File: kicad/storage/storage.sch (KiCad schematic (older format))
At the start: 8 parts, among them J1 Conn_02x30_Counter_Clockwise, J6 Conn_01x01, U1 7400, U2 7400, U3 Conn_02x08_Counter_Clockwise

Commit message: Finish storage card
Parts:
- removed J6: Conn_01x01, Connector_PinHeader_2.54mm:PinHeader_1x01_P2.54mm_Vertical, symbol Connector_Generic:Conn_01x01
- added J6: Conn_01x03, Connector_PinHeader_2.54mm:PinHeader_1x03_P2.54mm_Vertical, symbol Connector_Generic:Conn_01x03
- added J7: Conn_01x02, Connector_PinHeader_2.54mm:PinHeader_1x02_P2.54mm_Vertical, symbol Connector_Generic:Conn_01x02
- added R1, R2: R, Resistor_THT:R_Axial_DIN0207_L6.3mm_D2.5mm_P10.16mm_Horizontal, symbol Device:R
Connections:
- net GND: now also J6.1 (Pin_1)
- net WR: now also J1.38 (Pin_38)
- new net: J6.2 (Pin_2), R1.1
- new net: J6.3 (Pin_3), R2.1
- new net: J7.2 (Pin_2), R1.2
- new net: J7.1 (Pin_1), R2.2
- no-connect marks 38 -> 37
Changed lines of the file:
@@
 NoConn ~ 10100 4500
 NoConn ~ 10100 4400
-NoConn ~ 10100 4300
 NoConn ~ 10100 2800
 NoConn ~ 10100 3000
@@
 NoConn ~ 9600 4900
 $Comp
-L Connector_Generic:Conn_01x01 J6
-U 1 1 60BD2C0A
-P 1350 1400
-F 0 "J6" H 1430 1442 50  0000 L CNN
-F 1 "Conn_01x01" H 1430 1351 50  0000 L CNN
-F 2 "Connector_PinHeader_2.54mm:PinHeader_1x01_P2.54mm_Vertical" H 1350 1400 50  0001 C CNN
-F 3 "~" H 1350 1400 50  0001 C CNN
-	1    1350 1400
-	1    0    0    -1
-$EndComp
-Text GLabel 1150 1400 0    50   Input ~ 0
-WR
-$Comp
 L 74xx:7400 U1
 U 2 1 60BD3C08
@@
 Wire Wire Line
 	3150 7300 3450 7300
+Text GLabel 10100 4300 2    50   Input ~ 0
+WR
+$Comp
+L Connector_Generic:Conn_01x03 J6
+U 1 1 60C409E1
+P 2750 1500
+F 0 "J6" H 2830 1542 50  0000 L CNN
+F 1 "Conn_01x03" H 2830 1451 50  0000 L CNN
+F 2 "Connector_PinHeader_2.54mm:PinHeader_1x03_P2.54mm_Vertical" H 2750 1500 50  0001 C CNN
+F 3 "~" H 2750 1500 50  0001 C CNN
+	1    2750 1500
+	1    0    0    -1
+$EndComp
+Text GLabel 2550 1400 0    50   Input ~ 0
+GND
+$Comp
+L Device:R R1
+U 1 1 60C52E56
+P 2400 1500
+F 0 "R1" V 2193 1500 50  0000 C CNN
+F 1 "R" V 2284 1500 50  0000 C CNN
+F 2 "Resistor_THT:R_Axial_DIN0207_L6.3mm_D2.5mm_P10.16mm_Horizontal" V 2330 1500 50  0001 C CNN
+F 3 "~" H 2400 1500 50  0001 C CNN
+	1    2400 1500
+	0    1    1    0
+$EndComp
+$Comp
+L Device:R R2
+U 1 1 60C5383C
+P 2400 1600
+F 0 "R2" V 2193 1600 50  0000 C CNN
+F 1 "R" V 2284 1600 50  0000 C CNN
+F 2 "Resistor_THT:R_Axial_DIN0207_L6.3mm_D2.5mm_P10.16mm_Horizontal" V 2330 1600 50  0001 C CNN
+F 3 "~" H 2400 1600 50  0001 C CNN
+	1    2400 1600
+	0    1    1    0
+$EndComp
+$Comp
+L Connector_Generic:Conn_01x02 J7
+U 1 1 60C55150
+P 2050 1600
+F 0 "J7" H 1968 1275 50  0000 C CNN
+F 1 "Conn_01x02" H 1968 1366 50  0000 C CNN
+F 2 "Connector_PinHeader_2.54mm:PinHeader_1x02_P2.54mm_Vertical" H 2050 1600 50  0001 C CNN
+F 3 "~" H 2050 1600 50  0001 C CNN
+	1    2050 1600
+	-1   0    0    1
+$EndComp
 $EndSCHEMATC

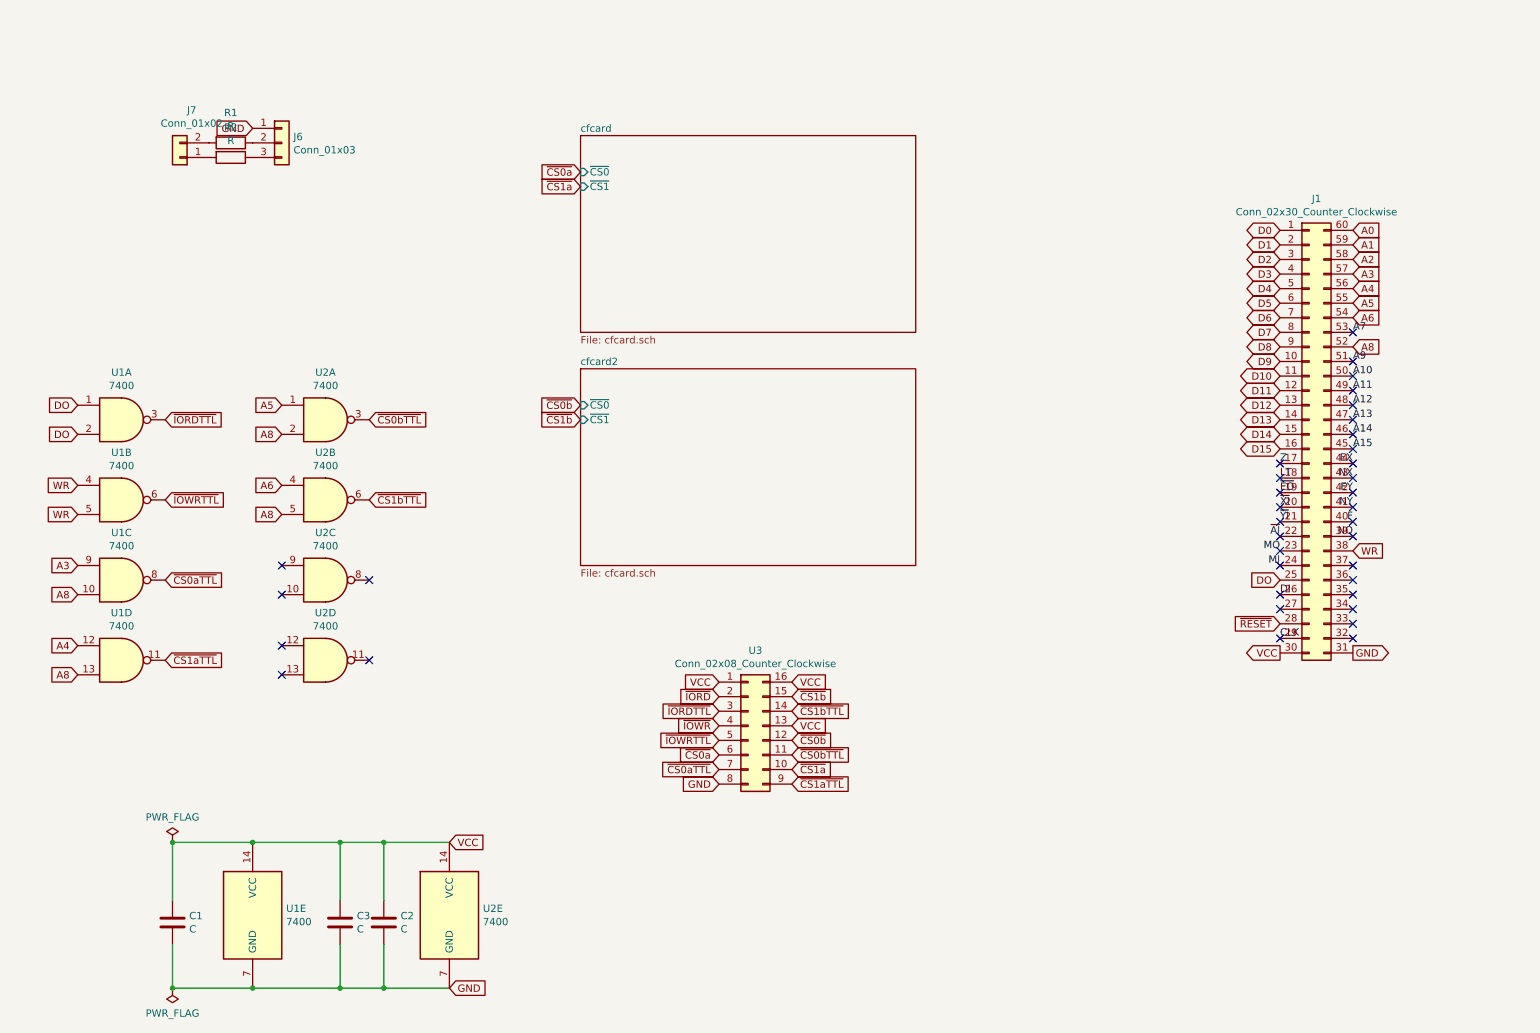
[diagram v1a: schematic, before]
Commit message: Add 74HCT245 bus transceivers to storage card
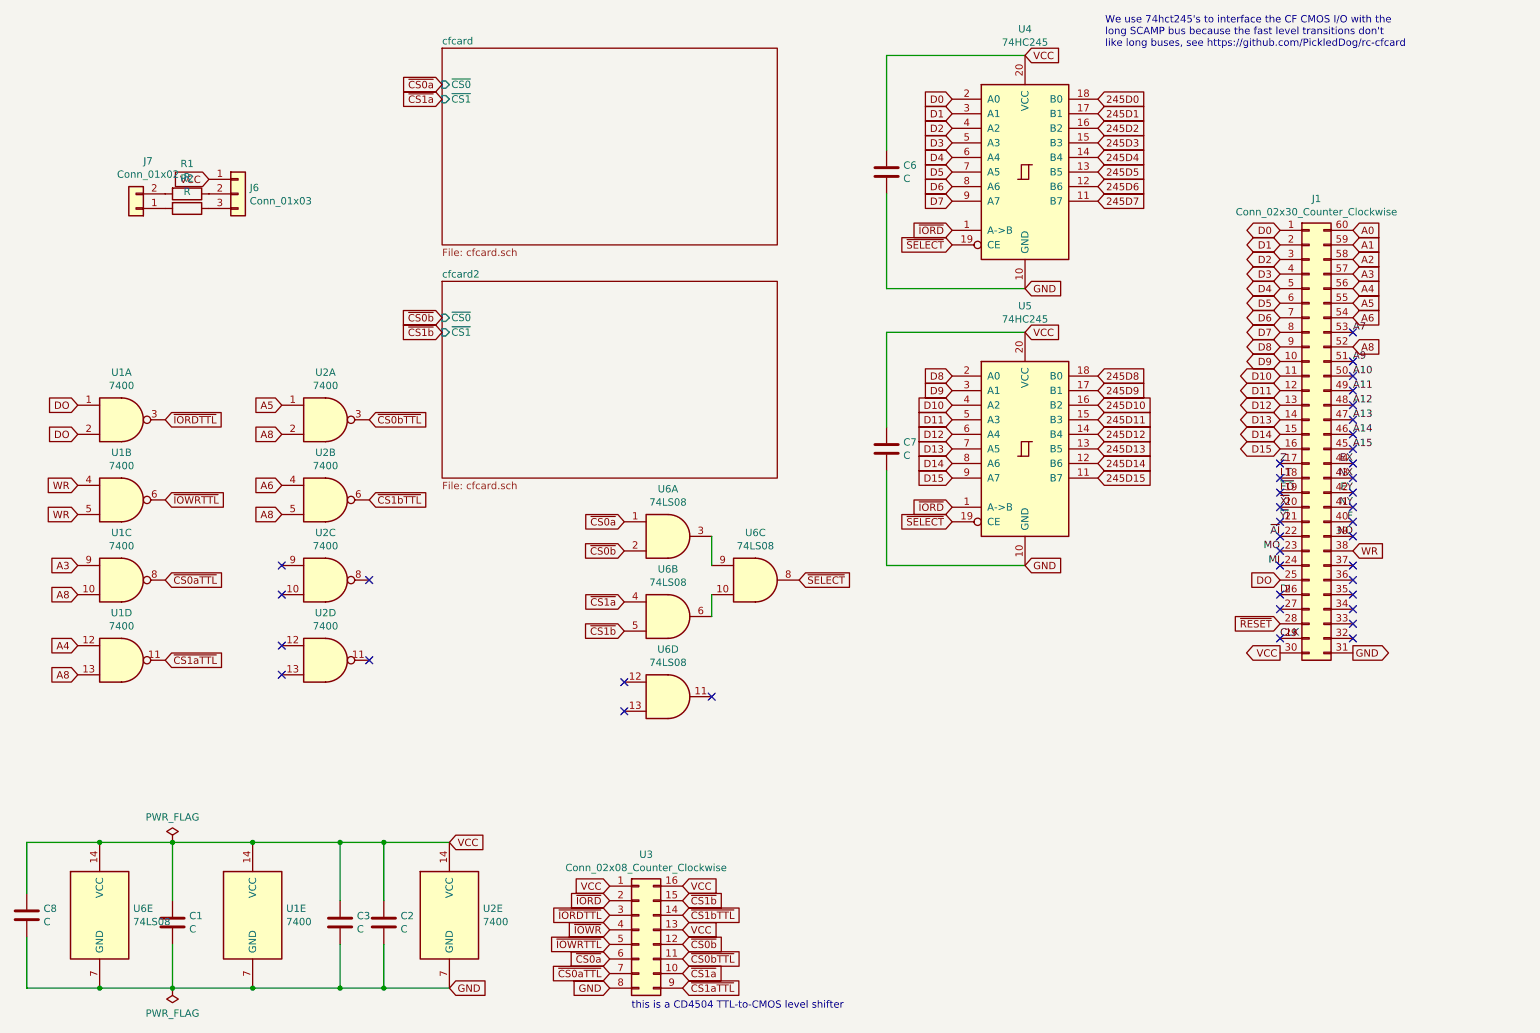
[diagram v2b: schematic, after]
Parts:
- added C6, C7, C8: C, Capacitor_THT:C_Disc_D6.0mm_W2.5mm_P5.00mm, symbol Device:C
- added U4, U5: 74HC245, Package_DIP:DIP-20_W7.62mm_Socket, symbol 74xx:74HC245
- added U6: 74LS08, Package_DIP:DIP-14_W7.62mm_Socket, symbol 74xx:74LS08
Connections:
- net D0: now also U4.2 (A0)
- net D1: now also U4.3 (A1)
- net D10: now also U5.4 (A2)
- net D11: now also U5.5 (A3)
- net D12: now also U5.6 (A4)
- net D13: now also U5.7 (A5)
- net D14: now also U5.8 (A6)
- net D15: now also U5.9 (A7)
- net D2: now also U4.4 (A2)
- net D3: now also U4.5 (A3)
- net D4: now also U4.6 (A4)
- net D5: now also U4.7 (A5)
- net D6: now also U4.8 (A6)
- net D7: now also U4.9 (A7)
- net D8: now also U5.2 (A0)
- net D9: now also U5.3 (A1)
- net GND: now also C6.2, C7.2, C8.2, U4.10 (GND), U5.10 (GND), U6.7 (GND); no longer J6.1 (Pin_1)
- net VCC: now also J6.1 (Pin_1), C6.1, C7.1, C8.1, U4.20 (VCC), U5.20 (VCC), U6.14 (VCC)
- net ~CS0a~: now also U6.1
- net ~CS0b~: now also U6.2
- net ~CS1a~: now also U6.4
- net ~CS1b~: now also U6.5
- net ~IORD~: now also U4.1 (A->B), U5.1 (A->B)
- new net: U6.3, U6.9
- new net: U6.10, U6.6
- new net 245D0: U4.18 (B0)
- new net 245D1: U4.17 (B1)
- new net 245D10: U5.16 (B2)
- new net 245D11: U5.15 (B3)
- new net 245D12: U5.14 (B4)
- new net 245D13: U5.13 (B5)
- new net 245D14: U5.12 (B6)
- new net 245D15: U5.11 (B7)
- new net 245D2: U4.16 (B2)
- new net 245D3: U4.15 (B3)
- new net 245D4: U4.14 (B4)
- new net 245D5: U4.13 (B5)
- new net 245D6: U4.12 (B6)
- new net 245D7: U4.11 (B7)
- new net 245D8: U5.18 (B0)
- new net 245D9: U5.17 (B1)
- new net ~SELECT~: U4.19 (CE), U5.19 (CE), U6.8
- no-connect marks 37 -> 40
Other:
- note added: "We use 74hct245's to interface the CF CMOS I/O with the\nlong SCAMP bus because the fast level transitions don't\nlike long buses, see https://github.com/PickledDog/rc-cfcard"
- note added: "this is a CD4504 TTL-to-CMOS level shifter"
- moved on the sheet: J6, R1, R2, U3
